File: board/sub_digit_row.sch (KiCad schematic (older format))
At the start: 83 parts, among them Q601 Q_PMOS_GSD, Q602 Q_PMOS_GSD, Q603 Q_PMOS_GSD, Q604 Q_PMOS_GSD, Q605 Q_PMOS_GSD, Q606 Q_PMOS_GSD, Q607 Q_PMOS_GSD, Q608 Q_PMOS_GSD, U601 TPIC6D595, U602 TPIC6D595, U603 TPIC6D595

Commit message: More Schematic progress
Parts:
- removed R601, R602, R604, R605, R607, R608: 120, symbol Device:R
- added C601, C602, C603: 1u, symbol Device:C
- added R620, R623, R637, R640, R654, R657: 100, symbol Device:R
- R609, R610, R611, R612, R613, R614, R615, R616, R617, R618, R619, R621, R622, R624, R625, R626, R627, R628, R629, R630, R631, R632, R633, R634, R635, R636, R638, R639, R641, R642, R643, R644, R645, R646, R647, R648, R649, R650, R651, R652, R653, R655, R656, R658, R659, R660, R661, R662, R663, R664, R665, R666, R667, R668: value 120 -> 100
- renumbered R603 to R601, R606 to R602, R620 to R603, R623 to R604, R637 to R605, R640 to R606, R654 to R607, R657 to R608
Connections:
- net +5V: now also C601.1, C602.1, C603.1
- net GND: now also C601.2, C602.2, C603.2
- net at D601.1 (E): now also R609.1
- net at D601.2 (N): now also R610.1
- net at D602.1 (E): now also R624.1; no longer R618.1
- net at D602.10 (B): now also R632.1; no longer R628.1
- net at D602.12 (A): now also R633.1; no longer R629.1
- net at D602.13 (G1): now also R634.1; no longer R630.1
- net at D602.14 (K): now also R635.1; no longer R631.1
- net at D602.15 (J): now also R636.1; no longer R632.1
- net at D602.17 (H): now also R637.1; no longer R633.1
- net at D602.18 (F): now also R638.1; no longer R634.1
- net at D602.2 (N): now also R625.1; no longer R619.1
- net at D602.4 (M): now also R626.1; no longer R621.1
- net at D602.5 (L): now also R627.1; no longer R622.1
- net at D602.6 (G2): now also R628.1; no longer R624.1
- net at D602.7 (D): now also R629.1; no longer R625.1
- net at D602.8 (DP): now also R630.1; no longer R626.1
- net at D602.9 (C): now also R631.1; no longer R627.1
- net at D603.1 (E): now also R639.1; no longer R635.1
- net at D603.10 (B): now also R647.1; no longer R645.1
- net at D603.12 (A): now also R648.1; no longer R646.1
- net at D603.13 (G1): now also R649.1; no longer R647.1
- net at D603.14 (K): now also R650.1; no longer R648.1
- net at D603.15 (J): now also R651.1; no longer R649.1
- net at D603.17 (H): now also R652.1; no longer R650.1
- net at D603.18 (F): now also R653.1; no longer R651.1
- net at D603.2 (N): now also R640.1; no longer R636.1
- net at D603.4 (M): now also R641.1; no longer R638.1
- net at D603.5 (L): now also R642.1; no longer R639.1
- net at D603.6 (G2): now also R643.1; no longer R641.1
- net at D603.7 (D): now also R644.1; no longer R642.1
- net at D603.8 (DP): now also R645.1; no longer R643.1
- net at D603.9 (C): now also R646.1; no longer R644.1
- net at D604.1 (E): now also R654.1; no longer R652.1
- net at D604.2 (N): now also R655.1; no longer R653.1
- net at D604.4 (M): now also R656.1; no longer R655.1
- net at D604.5 (L): now also R657.1; no longer R656.1
- net at D601.10 (B): now also R617.1; no longer R611.1
- net at D601.12 (A): now also R618.1; no longer R612.1
- net at D601.13 (G1): now also R619.1; no longer R613.1
- net at D601.14 (K): now also R620.1; no longer R614.1
- net at D601.15 (J): now also R621.1; no longer R615.1
- net at D601.17 (H): now also R622.1; no longer R616.1
- net at D601.18 (F): now also R623.1; no longer R617.1
- net at D601.4 (M): now also R611.1
- net at D601.5 (L): now also R612.1
- net at D601.6 (G2): now also R613.1
- net at D601.7 (D): now also R614.1
- net at D601.8 (DP): now also R615.1; no longer R609.1
- net at D601.9 (C): now also R616.1; no longer R610.1
- net at R658.2, U602.11 (DRAIN4): now also R613.2, R628.2, R643.2; no longer R624.2, R641.2
- net at R659.2, U602.12 (DRAIN5): now also R614.2, R629.2, R644.2; no longer R625.2, R642.2
- new net: R621.2, R636.2, R651.2, R666.2, U603.11 (DRAIN4)
- new net: R622.2, R637.2, R652.2, R667.2, U603.12 (DRAIN5)
- new net: R623.2, R638.2, R653.2, R668.2, U603.13 (DRAIN6)
- new net: R617.2, R632.2, R647.2, R662.2, U603.3 (DRAIN0)
- new net: R618.2, R633.2, R648.2, R663.2, U603.4 (DRAIN1)
- new net: R619.2, R634.2, R649.2, R664.2, U603.5 (DRAIN2)
- new net: R620.2, R635.2, R650.2, R665.2, U603.6 (DRAIN3)
- new net: R615.2, R630.2, R645.2, R660.2, U602.13 (DRAIN6)
- new net: R616.2, R631.2, R646.2, R661.2, U602.14 (DRAIN7)
- new net: R609.2, R624.2, R639.2, R654.2, U602.3 (DRAIN0)
- new net: R610.2, R625.2, R640.2, R655.2, U602.4 (DRAIN1)
- new net: R611.2, R626.2, R641.2, R656.2, U602.5 (DRAIN2)
- new net: R612.2, R627.2, R642.2, R657.2, U602.6 (DRAIN3)
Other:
- moved on the sheet: D701, D702, D703, D704, Q701, Q702, Q703, Q704, Q705, Q706, Q707, Q708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

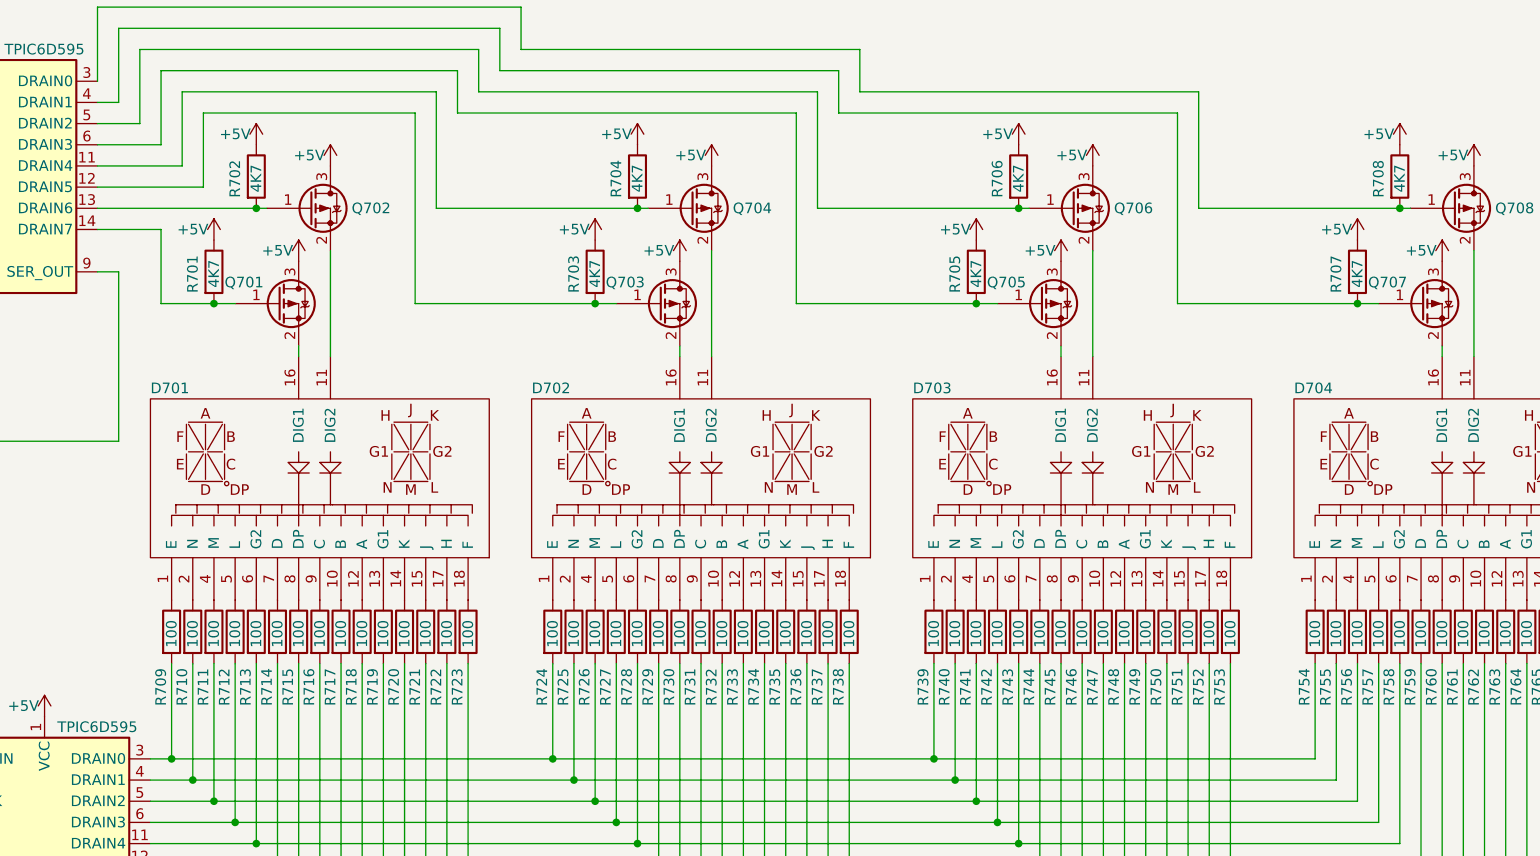
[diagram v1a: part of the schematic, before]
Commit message: Bus signal connectivity rebuilt
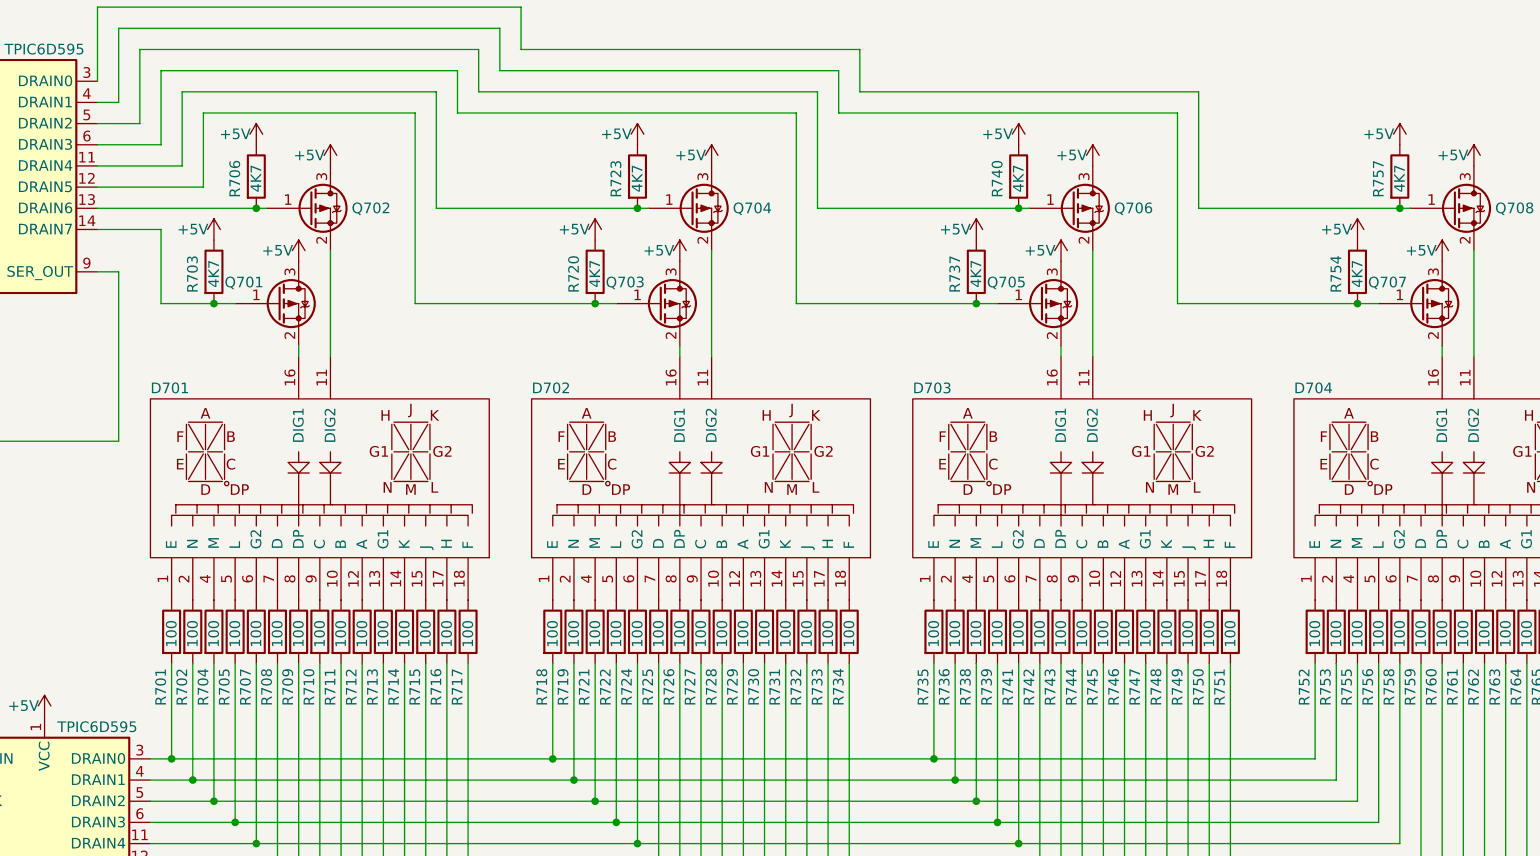
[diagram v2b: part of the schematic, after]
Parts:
- renumbered R609 to R601, R610 to R602, R601 to R603, R611 to R604, R612 to R605, R602 to R606, R613 to R607, R614 to R608, R615 to R609, R616 to R610, R617 to R611, R618 to R612, R619 to R613, R620 to R614, R621 to R615, R622 to R616, R623 to R617, R624 to R618, R625 to R619, R603 to R620, R626 to R621, R627 to R622, R604 to R623, R628 to R624, R629 to R625, R630 to R626, R631 to R627, R632 to R628, R633 to R629, R634 to R630, R635 to R631, R636 to R632, R637 to R633, R638 to R634, R639 to R635, R640 to R636, R605 to R637, R641 to R638, R642 to R639, R606 to R640, R643 to R641, R644 to R642, R645 to R643, R646 to R644, R647 to R645, R648 to R646, R649 to R647, R650 to R648, R651 to R649, R652 to R650, R653 to R651, R654 to R652, R655 to R653, R607 to R654, R656 to R655, R657 to R656, R608 to R657

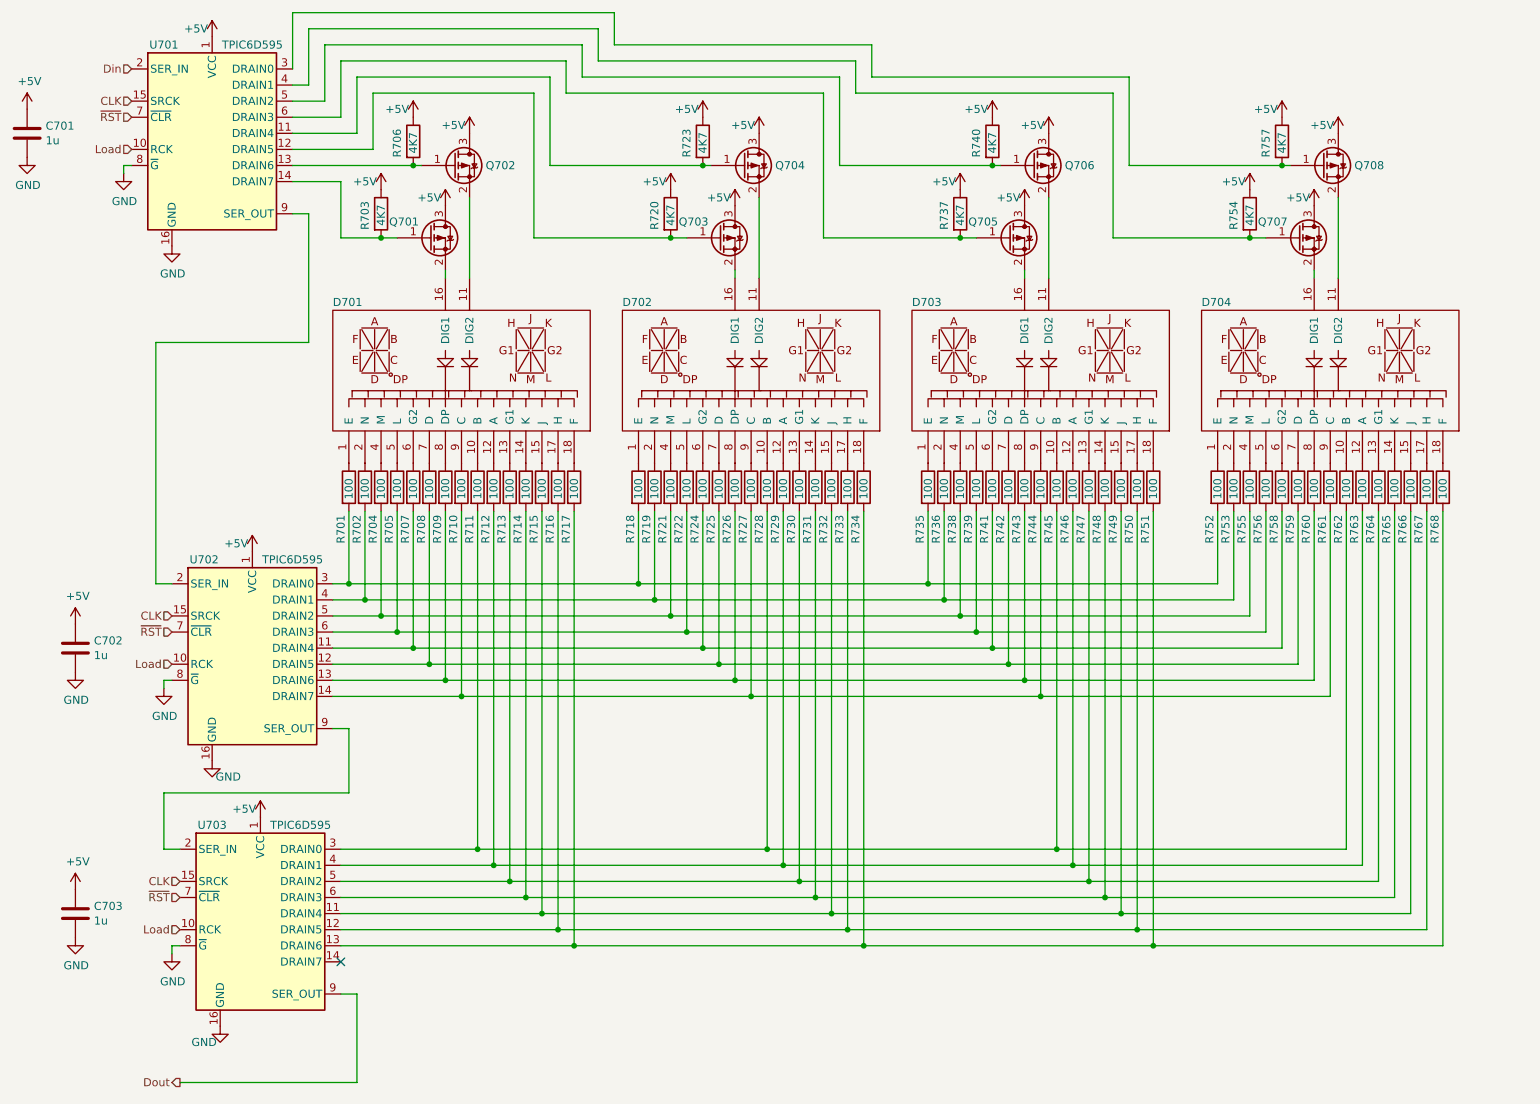
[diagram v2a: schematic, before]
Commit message: made some changes based on projected power budget
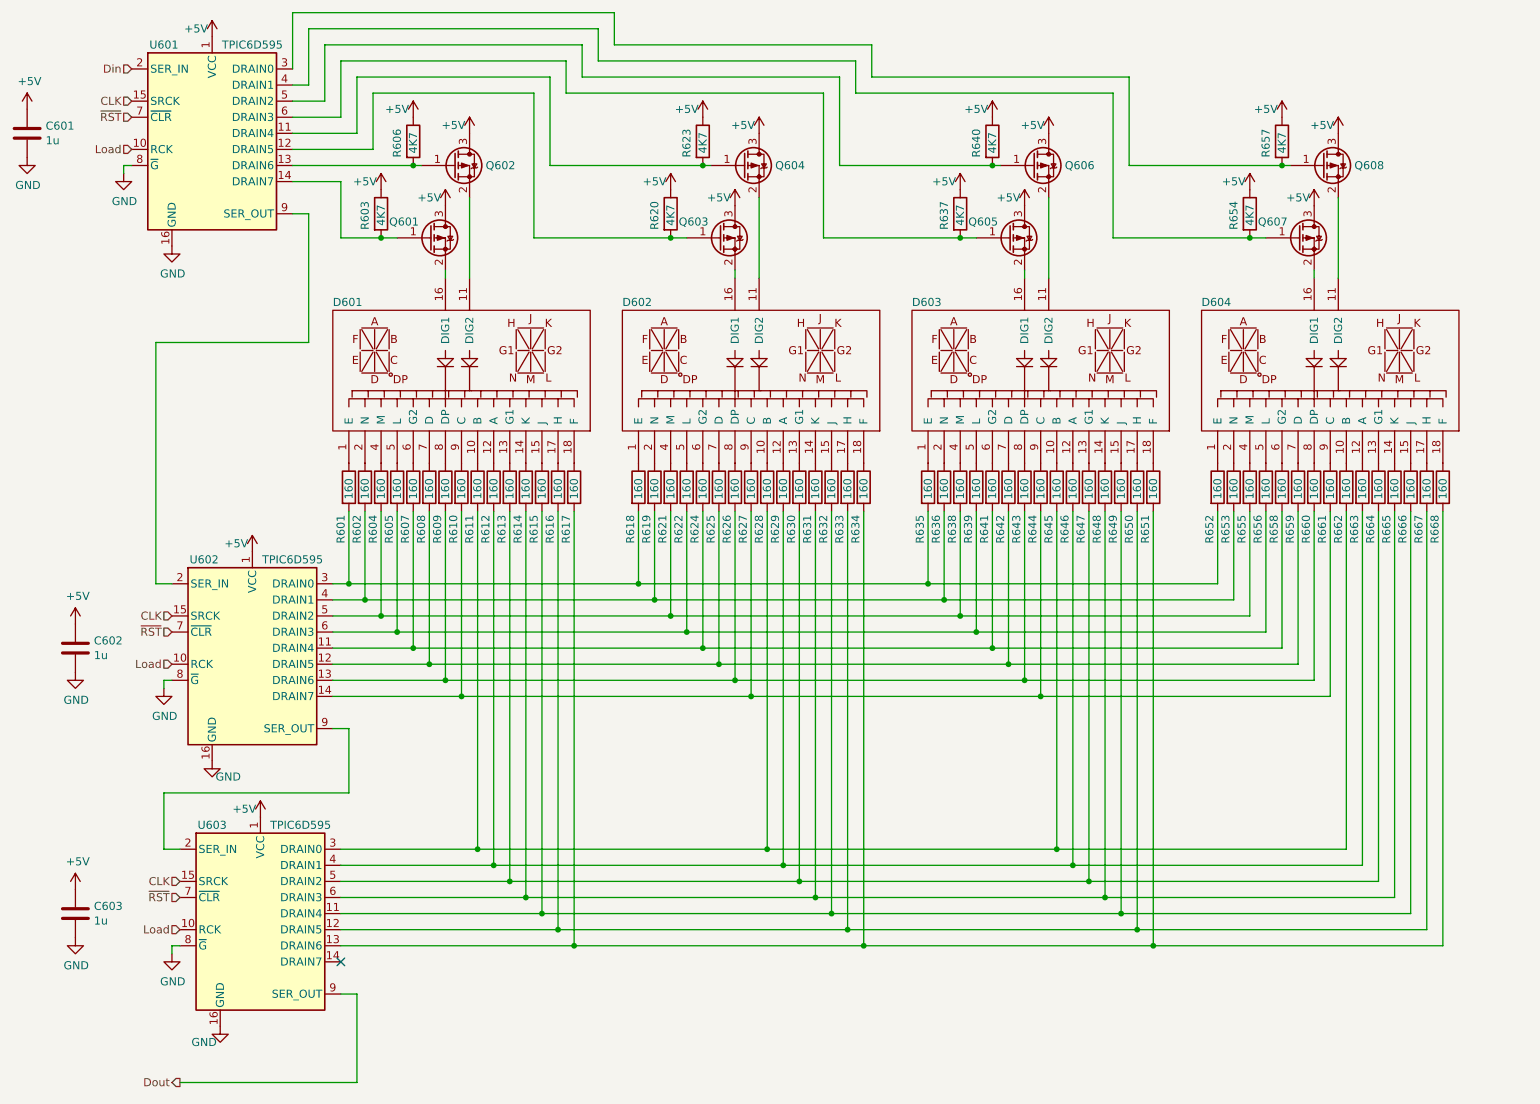
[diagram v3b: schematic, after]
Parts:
- R601, R602, R604, R605, R607, R608, R609, R610, R611, R612, R613, R614, R615, R616, R617, R618, R619, R621, R622, R624, R625, R626, R627, R628, R629, R630, R631, R632, R633, R634, R635, R636, R638, R639, R641, R642, R643, R644, R645, R646, R647, R648, R649, R650, R651, R652, R653, R655, R656, R658, R659, R660, R661, R662, R663, R664, R665, R666, R667, R668: value 100 -> 160

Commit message: Schematics mostly complete
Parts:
- renumbered Q602 to Q601, Q604 to Q602, Q606 to Q603, Q608 to Q604, Q601 to Q605, Q603 to Q606, Q605 to Q607, Q607 to Q608, R606 to R601, R623 to R602, R640 to R603, R657 to R604, R603 to R605, R620 to R606, R637 to R607, R654 to R608, R601 to R609, R602 to R610, R604 to R611, R605 to R612, R607 to R613, R608 to R614, R609 to R615, R610 to R616, R611 to R617, R612 to R618, R613 to R619, R614 to R620, R615 to R621, R616 to R622, R617 to R623, R618 to R624, R619 to R625, R621 to R626, R622 to R627, R624 to R628, R625 to R629, R626 to R630, R627 to R631, R628 to R632, R629 to R633, R630 to R634, R631 to R635, R632 to R636, R633 to R637, R634 to R638, R635 to R639, R636 to R640, R638 to R641, R639 to R642, R641 to R643, R642 to R644, R643 to R645, R644 to R646, R645 to R647, R646 to R648, R647 to R649, R648 to R650, R649 to R651, R650 to R652, R651 to R653, R652 to R654, R653 to R655, R655 to R656, R656 to R657
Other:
- moved on the sheet: R709, R710, R711, R712, R713, R714, R715, R716, R717, R718, R719, R720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
